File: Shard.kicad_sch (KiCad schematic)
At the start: 39 parts, among them J1 USB_C_Receptacle_USB2.0_16P, J2 Conn_01x02_Pin, SW1 SW_Push, SW2 SW_Push, U1 ESP32-S3, U2 USBLC6-2P6, U3 TLV76733DRVx, U4 TLV76733DRVx, U5 W25Q128JVS

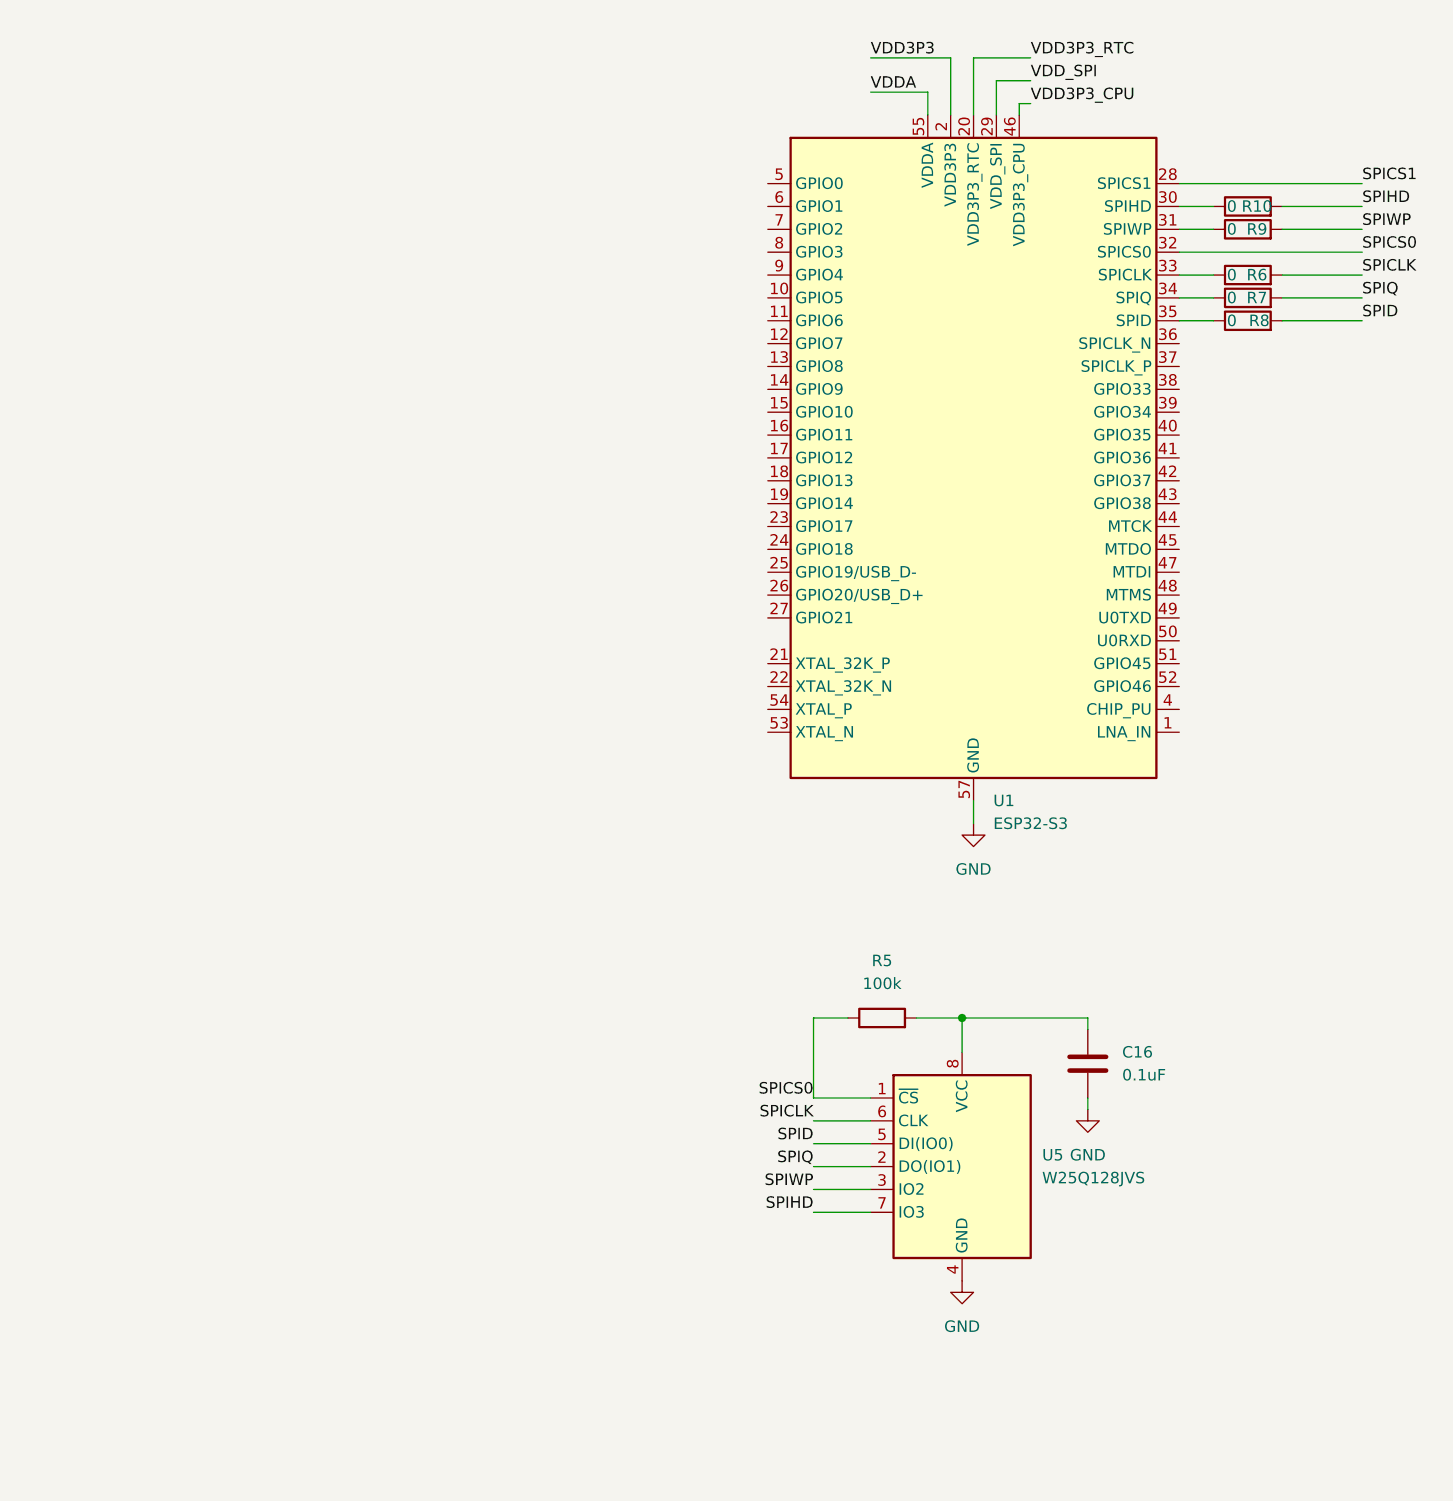
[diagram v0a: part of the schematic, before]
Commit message: Add Crystal Oscillator.
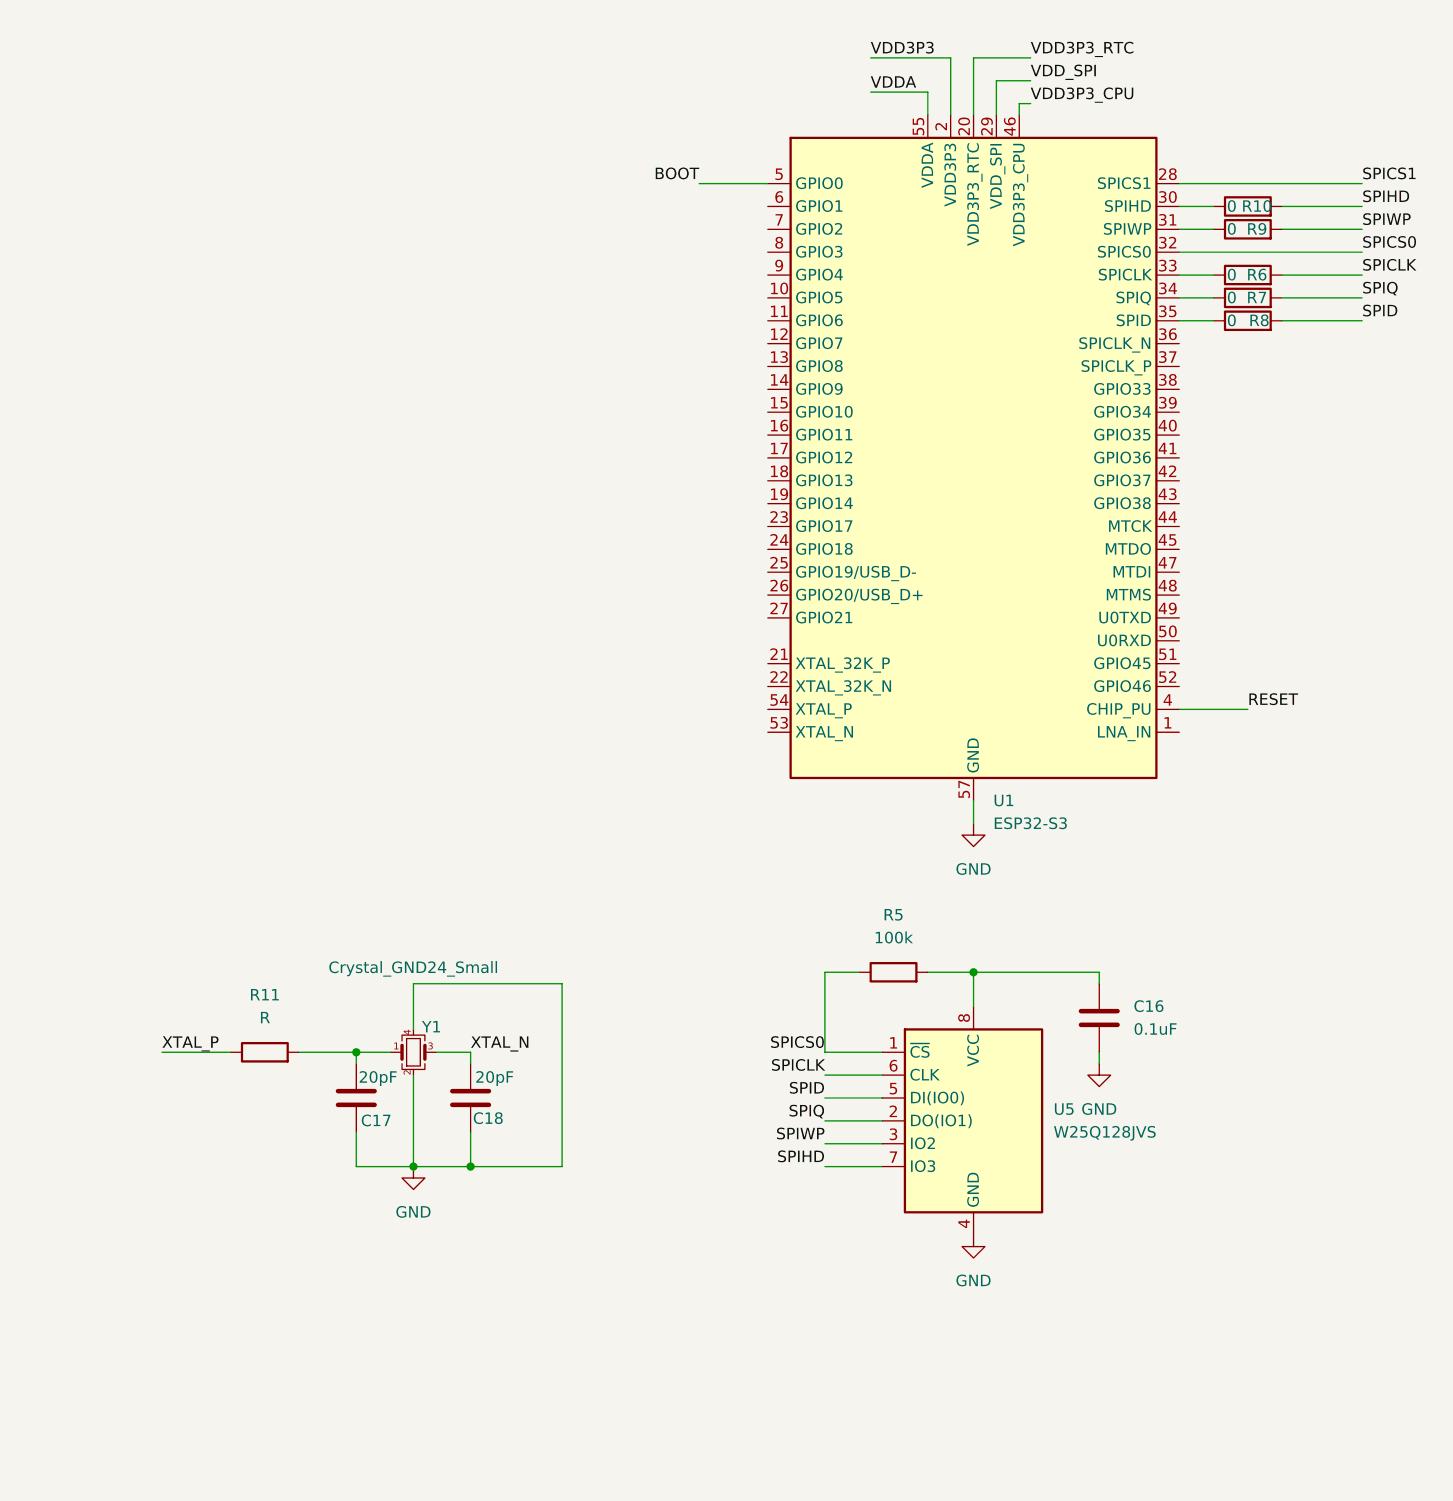
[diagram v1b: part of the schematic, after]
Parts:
- added C17, C18: 20pF, symbol Device:C
- added R11: R, symbol Device:R
- added Y1: Crystal_GND24_Small, Crystal:Crystal_SMD_2520-4Pin_2.5x2.0mm, symbol Device:Crystal_GND24_Small
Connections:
- net BOOT: now also U1.5 (GPIO0)
- net GND: now also C17.2, C18.2, Y1.2, Y1.4
- net RESET: now also U1.4 (CHIP_PU)
- new net: C17.1, R11.2, Y1.1
- new net XTAL_N: C18.1, Y1.3
- new net XTAL_P: R11.1
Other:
- moved on the sheet: C16, R5, U5

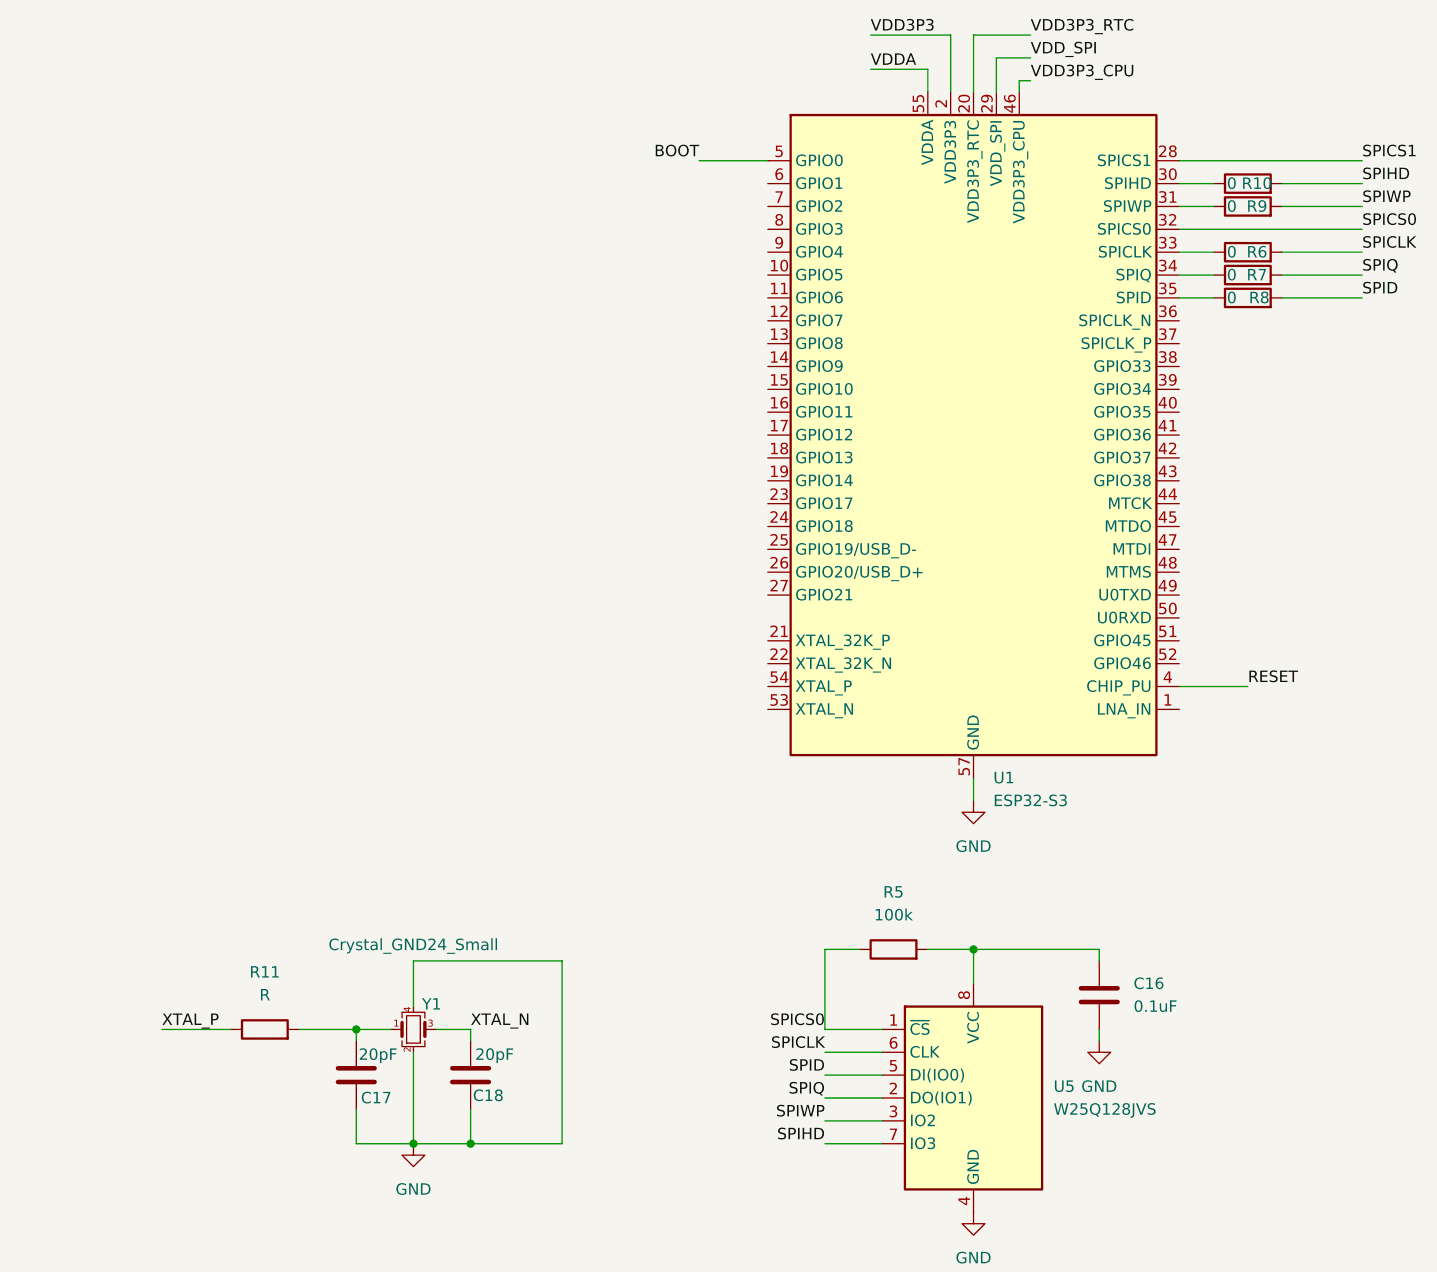
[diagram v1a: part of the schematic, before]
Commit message: Finish crystal scheme, started GPIO labeling
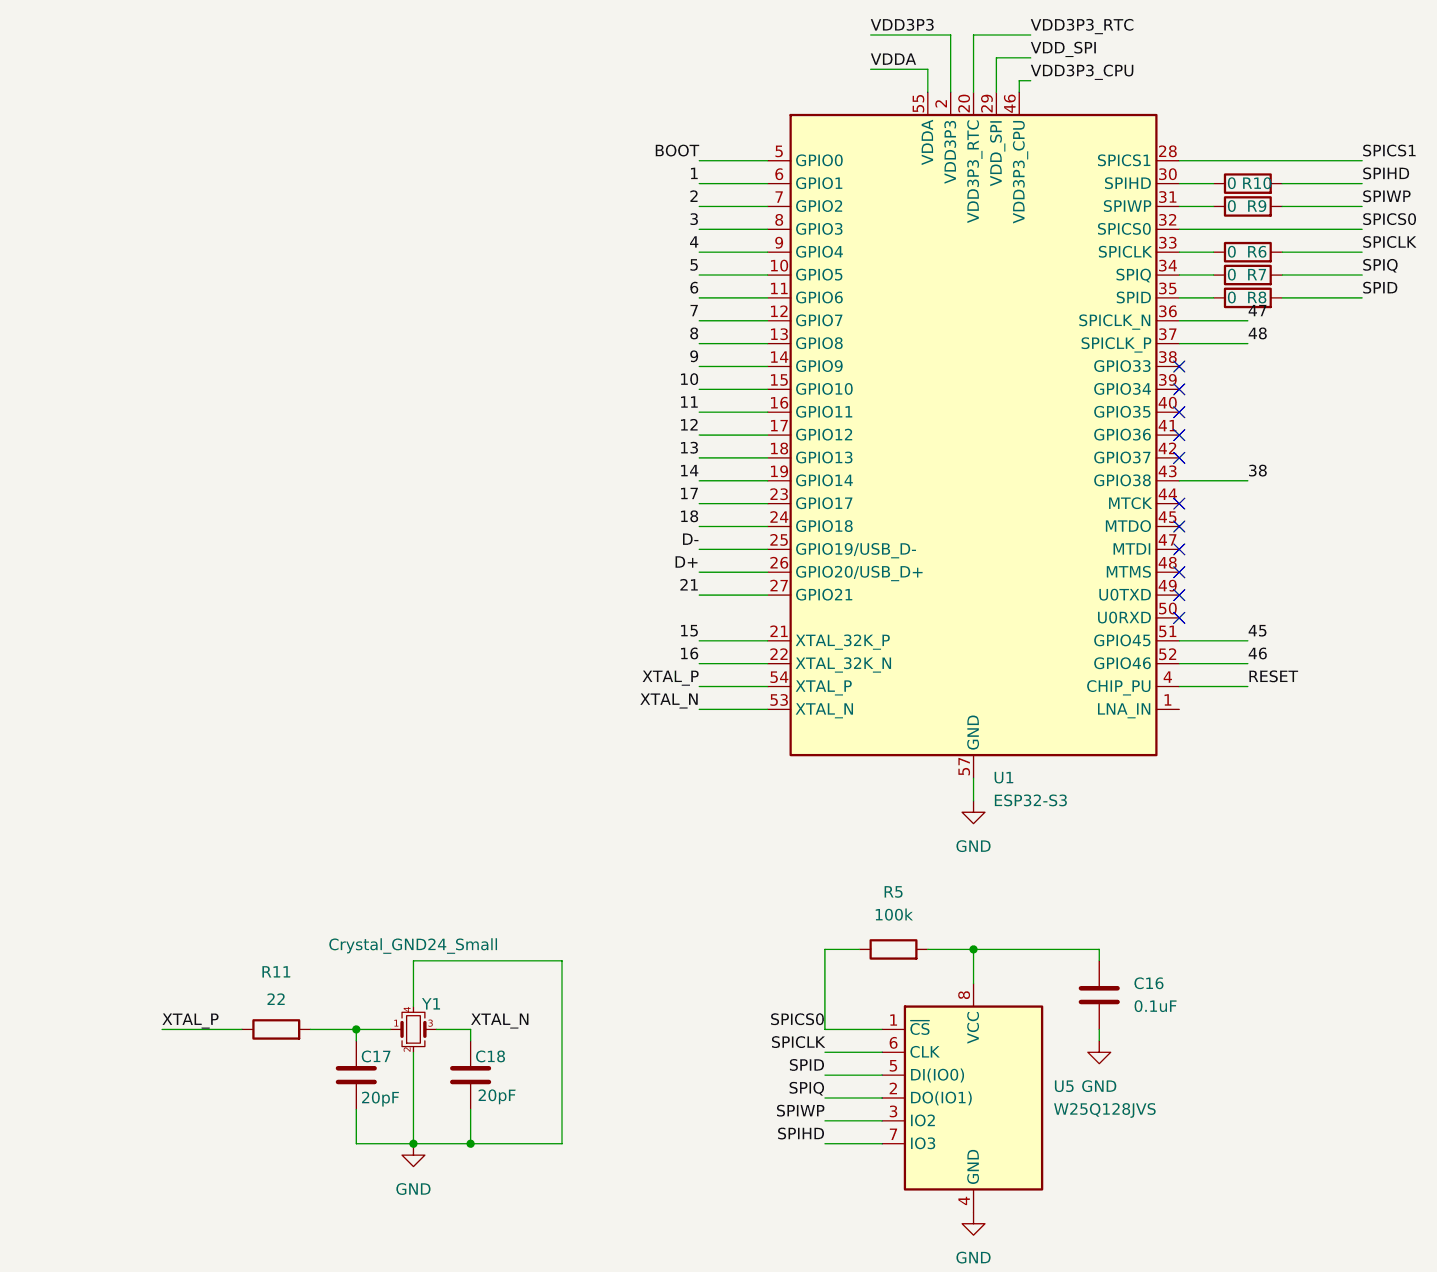
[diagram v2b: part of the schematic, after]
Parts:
- R11: value R -> 22; footprint (none) -> Resistor_SMD:R_0805_2012Metric; REF (none) -> C2933536
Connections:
- net D+: now also U1.26 (GPIO20/USB_D+)
- net D-: now also U1.25 (GPIO19/USB_D-)
- net XTAL_N: now also U1.53 (XTAL_N)
- net XTAL_P: now also U1.54 (XTAL_P)
- net 5: now reaches U1.10 (GPIO5)
- net 6: now reaches U1.11 (GPIO6)
- net 7: now reaches U1.12 (GPIO7)
- net 8: now reaches U1.13 (GPIO8)
- net 9: now reaches U1.14 (GPIO9)
- net 10: now reaches U1.15 (GPIO10)
- net 11: now reaches U1.16 (GPIO11)
- net 12: now reaches U1.17 (GPIO12)
- net 13: now reaches U1.18 (GPIO13)
- net 14: now reaches U1.19 (GPIO14)
- net 15: now reaches U1.21 (XTAL_32K_P)
- net 16: now reaches U1.22 (XTAL_32K_N)
- net 17: now reaches U1.23 (GPIO17)
- net 18: now reaches U1.24 (GPIO18)
- net 21: now reaches U1.27 (GPIO21)
- net 47: now reaches U1.36 (SPICLK_N)
- net 48: now reaches U1.37 (SPICLK_P)
- net 38: now reaches U1.43 (GPIO38)
- net 45: now reaches U1.51 (GPIO45)
- net 46: now reaches U1.52 (GPIO46)
- net 1: now reaches U1.6 (GPIO1)
- net 2: now reaches U1.7 (GPIO2)
- net 3: now reaches U1.8 (GPIO3)
- net 4: now reaches U1.9 (GPIO4)
- no-connect marks 3 -> 14
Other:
- moved on the sheet: R11
